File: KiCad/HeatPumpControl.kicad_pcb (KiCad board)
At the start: 2 copper layers, 38.2 x 37.4 mm, 45 parts, among them J1 Conn_01x04_Male, J2 Conn_01x04_Male, J3 Conn_01x04_Male, J4 Conn_01x03_Male, Q1 2N2222A, Q2 Q_PMOS_GDS, U3 XIAO-ESP32-C6-SMD

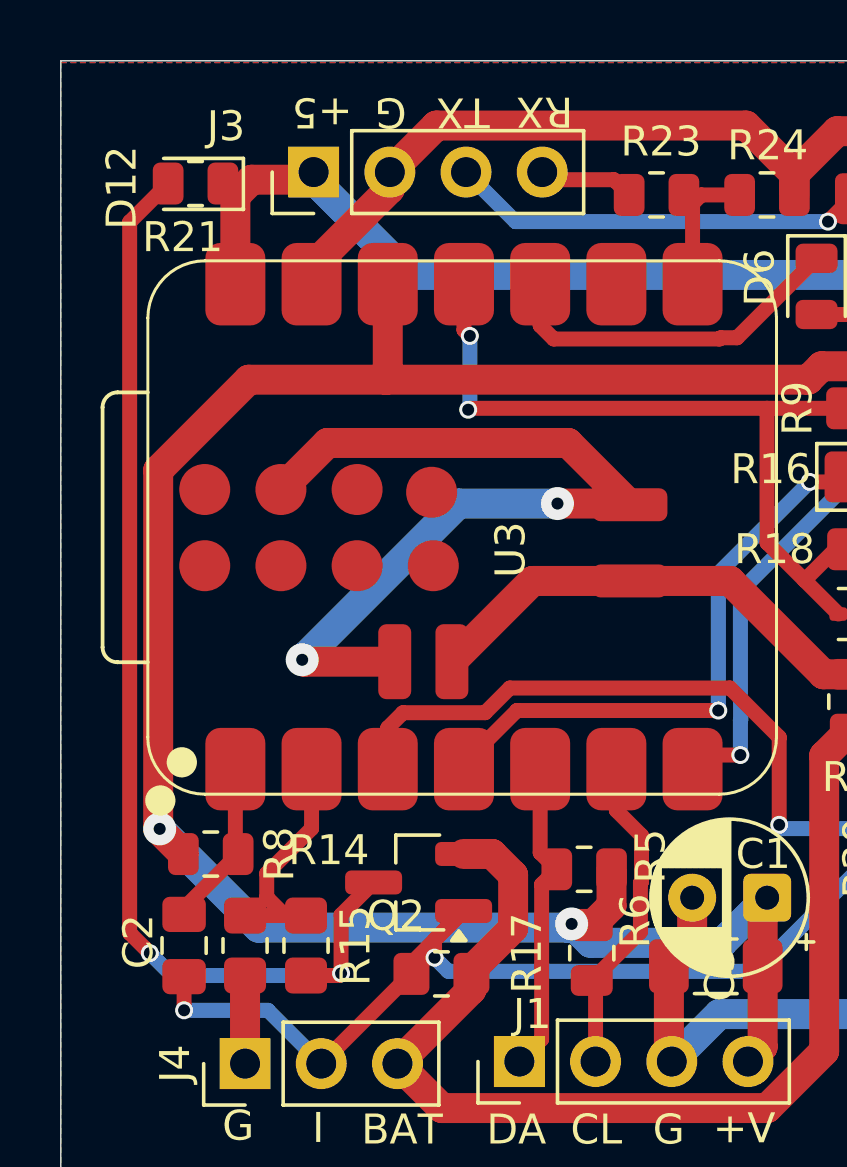
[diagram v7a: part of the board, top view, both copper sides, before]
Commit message: Change to SOD-123 for 1N4007
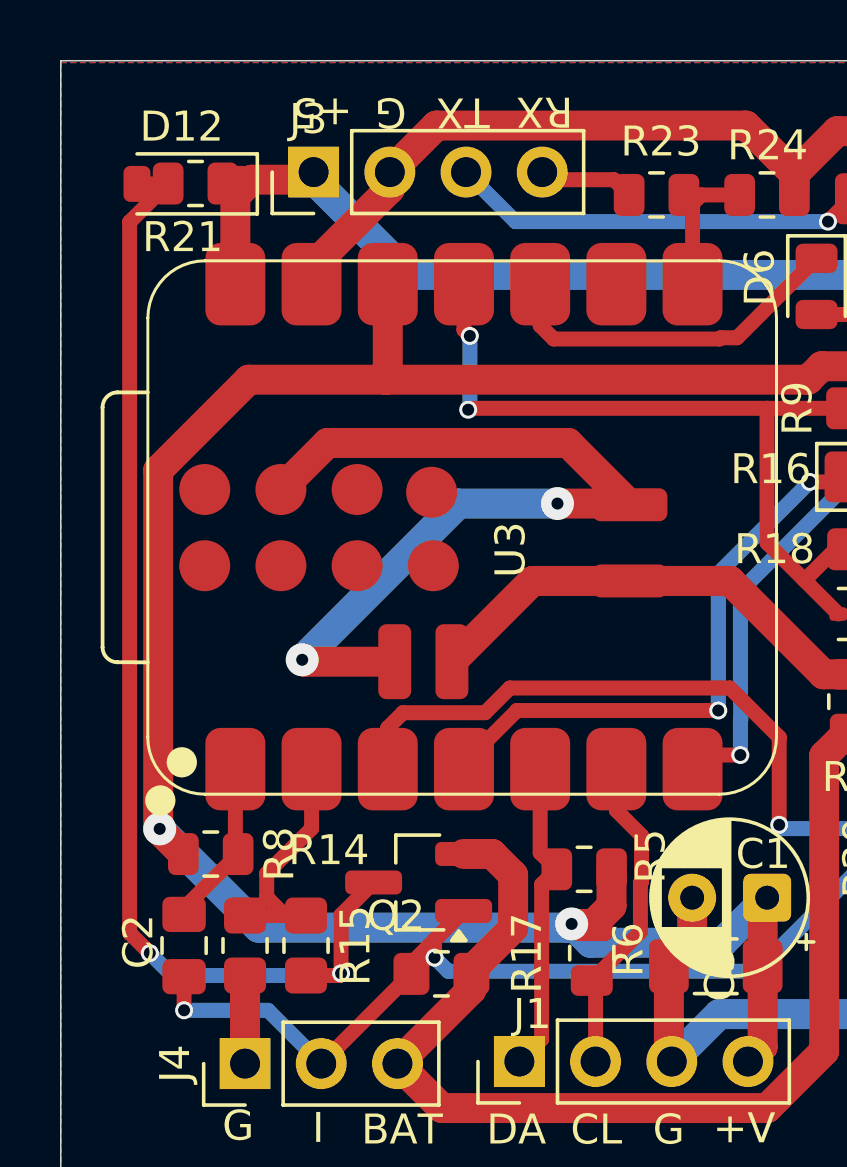
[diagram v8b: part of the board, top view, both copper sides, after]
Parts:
- D12: footprint Diode_SMD:D_SOD-323 -> Diode_SMD:D_SOD-123
- moved D12 0.29 mm to (140.1, 90.6)
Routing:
- net Net-(D12-A): track 37.9 -> 38.9 mm
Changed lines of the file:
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@@
 	(title_block
 		(title "Heath pump ctrl / generic IO")
-		(date "2025-12-04")
-		(rev "4.0.2")
+		(date "2025-12-23")
+		(rev "4.0.3")
 		(company "Hans Rune Bue <email@hansrune.net>")
 		(comment 1 "PCB version 4.0.0 can be still be used")
@@
 		(tags "resistor")
 		(property "Reference" "R6"
-			(at -1.0733 -1.4543 90)
+			(at -0.1143 -1.2225 90)
 			(layer "F.SilkS")
 			(effects
@@
 		)
 	)
-	(footprint "Diode_SMD:D_SOD-323"
+	(footprint "Diode_SMD:D_SOD-123"
 		(layer "F.Cu")
-		(at 140.369 90.551 180)
-		(descr "SOD-323")
-		(tags "SOD-323")
+		(at 140.082 90.551 180)
+		(descr "SOD-123")
+		(tags "SOD-123")
 		(property "Reference" "D12"
-			(at 2.447 -0.127 90)
+			(at 0.161 1.905 180)
 			(layer "F.SilkS")
 			(effects
@@
 		)
 		(property "Value" "1N4007"
-			(at 0.1 1.9 0)
+			(at 0 2.1 180)
 			(layer "F.Fab")
 			(effects
@@
 		(attr smd)
 		(fp_line
-			(start -1.61 0.85)
-			(end 1.05 0.85)
+			(start -2.36 1)
+			(end 1.65 1)
 			(stroke
 				(width 0.12)
@@
 		)
 		(fp_line
-			(start -1.61 -0.85)
-			(end 1.05 -0.85)
+			(start -2.36 -1)
+			(end 1.65 -1)
 			(stroke
 				(width 0.12)
@@
 		)
 		(fp_line
-			(start -1.61 -0.85)
-			(end -1.61 0.85)
+			(start -2.36 -1)
+			(end -2.36 1)
 			(stroke
 				(width 0.12)
@@
 		)
 		(fp_line
-			(start 1.6 -0.95)
-			(end 1.6 0.95)
+			(start 2.35 1.15)
+			(end -2.35 1.15)
 			(stroke
 				(width 0.05)
@@
 		)
 		(fp_line
-			(start -1.6 0.95)
-			(end 1.6 0.95)
+			(start 2.35 -1.15)
+			(end 2.35 1.15)
 			(stroke
 				(width 0.05)
@@
 		)
 		(fp_line
-			(start -1.6 -0.95)
-			(end 1.6 -0.95)
+			(start -2.35 -1.15)
+			(end 2.35 -1.15)
 			(stroke
 				(width 0.05)
@@
 		)
 		(fp_line
-			(start -1.6 -0.95)
-			(end -1.6 0.95)
+			(start -2.35 -1.15)
+			(end -2.35 1.15)
 			(stroke
 				(width 0.05)
@@
 		)
 		(fp_line
-			(start 0.9 0.7)
-			(end -0.9 0.7)
+			(start 1.4 0.9)
+			(end -1.4 0.9)
 			(stroke
 				(width 0.1)
@@
 		)
 		(fp_line
-			(start 0.9 -0.7)
-			(end 0.9 0.7)
+			(start 1.4 -0.9)
+			(end 1.4 0.9)
 			(stroke
 				(width 0.1)
@@
 		)
 		(fp_line
-			(start 0.2 0.35)
-			(end -0.3 0)
+			(start 0.25 0.4)
+			(end -0.35 0)
 			(stroke
 				(width 0.1)
@@
 		)
 		(fp_line
-			(start 0.2 0)
-			(end 0.45 0)
+			(start 0.25 0)
+			(end 0.75 0)
 			(stroke
 				(width 0.1)
@@
 		)
 		(fp_line
-			(start 0.2 -0.35)
-			(end 0.2 0.35)
+			(start 0.25 -0.4)
+			(end 0.25 0.4)
 			(stroke
 				(width 0.1)
@@
 		)
 		(fp_line
-			(start -0.3 0)
-			(end 0.2 -0.35)
+			(start -0.35 0)
+			(end 0.25 -0.4)
 			(stroke
 				(width 0.1)
@@
 		)
 		(fp_line
-			(start -0.3 0)
-			(end -0.5 0)
+			(start -0.35 0)
+			(end -0.35 0.55)
 			(stroke
 				(width 0.1)
@@
 		)
 		(fp_line
-			(start -0.3 -0.35)
-			(end -0.3 0.35)
+			(start -0.35 0)
+			(end -0.35 -0.55)
 			(stroke
 				(width 0.1)
@@
 		)
 		(fp_line
-			(start -0.9 0.7)
-			(end -0.9 -0.7)
+			(start -0.75 0)
+			(end -0.35 0)
 			(stroke
 				(width 0.1)
@@
 		)
 		(fp_line
-			(start -0.9 -0.7)
-			(end 0.9 -0.7)
+			(start -1.4 0.9)
+			(end -1.4 -0.9)
+			(stroke
+				(width 0.1)
+				(type solid)
+			)
+			(layer "F.Fab")
+		)
+		(fp_line
+			(start -1.4 -0.9)
+			(end 1.4 -0.9)
 			(stroke
 				(width 0.1)
@@
 		)
 		(fp_text user "${REFERENCE}"
-			(at 0 -1.85 0)
+			(at 0 -2 180)
 			(layer "F.Fab")
 			(effects
@@
 		)
 		(pad "1" smd roundrect
-			(at -1.05 0 180)
-			(size 0.6 0.45)
+			(at -1.65 0 180)
+			(size 0.9 1.2)
 			(layers "F.Cu" "F.Mask" "F.Paste")
 			(roundrect_rratio 0.25)
@@
 		)
 		(pad "2" smd roundrect
-			(at 1.05 0 180)
-			(size 0.6 0.45)
+			(at 1.65 0 180)
+			(size 0.9 1.2)
 			(layers "F.Cu" "F.Mask" "F.Paste")
 			(roundrect_rratio 0.25)
@@
 		)
 		(embedded_fonts no)
-		(model "${KICAD9_3DMODEL_DIR}/Diode_SMD.3dshapes/D_SOD-323.step"
+		(model "${KICAD9_3DMODEL_DIR}/Diode_SMD.3dshapes/D_SOD-123.step"
 			(offset
 				(xyz 0 0 0)
@@
 		(tags "Through hole pin header THT 1x04 2.54mm single row")
 		(property "Reference" "J3"
-			(at 1.524 -2.921 180)
+			(at 1.7653 -0.1745 180)
 			(layer "F.SilkS")
 			(effects
@@
 	)
 	(segment
+		(start 138.187 91.8213)
+		(end 139.47 90.5383)
+		(width 0.5)
+		(layer "F.Cu")
+		(net 35)
+	)
+	(segment
 		(start 144.0655 116.9383)
 		(end 145.163627 116.9383)
@@
 	)
 	(segment
+		(start 138.432 90.551)
+		(end 139.4573 90.551)
+		(width 0.5)
+		(layer "F.Cu")
+		(net 35)
+	)
+	(segment
 		(start 145.163627 116.9383)
 		(end 145.234 116.867927)
@@
 	)
 	(segment
-		(start 139.47 90.5383)
-		(end 138.187 91.8213)
+		(start 139.4573 90.551)
+		(end 139.47 90.5383)
 		(width 0.5)
 		(layer "F.Cu")
@@
 		(min_thickness 0.254)
 		(filled_areas_thickness no)
-		(fill
+		(fill yes
 			(thermal_gap 0.508)
 			(thermal_bridge_width 0.508)
